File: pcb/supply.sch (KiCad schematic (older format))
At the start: 11 parts, among them J1 Barrel_Jack_Switch, J13 Conn_01x02_Female, U9 ZLDO1117G33TA

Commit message: added ice40 regulators
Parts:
- added C72, C76, C77: 33u, Capacitor_SMD:C_1206_3216Metric, symbol Device:C
- added C73: 10u, Capacitor_SMD:C_0805_2012Metric, symbol Device:C
- added C74, C75: 0.1u, Capacitor_SMD:C_0603_1608Metric, symbol Device:C
- added R2: 120, Resistor_SMD:R_0402_1005Metric, symbol Device:R
- added U18: ZLDO1117G33TA, SMD:SOT-223, symbol ZLDO1117G33TA:ZLDO1117G33TA
- added U19: ZLDO1117G12TA, symbol ZLDO1117G33TA:ZLDO1117G12TA
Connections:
- net labels added: 1V2_ICE, 3V3_ICE
- wire segments 21 -> 43
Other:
- note added: "1.2V ice40 regulator\n"
- note added: "3.3V ICE40 regulator\n"

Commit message: Added 3V3_STM in STM32F4 and supply sheets
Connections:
- net labels added: 3V3_STM
- net labels removed: 3V3_ESP
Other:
- note added: "STM regulator"
- note removed: "ESP32 regulator\n"
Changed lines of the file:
@@
 $EndComp
 Text Notes 9300 1050 0    50   ~ 0
-ESP32 regulator\n
+STM regulator
 $Comp
-L ventilator-PowerSymbols:3V3_ESP #PWR0165
+L ventilator-PowerSymbols:3V3_STM #PWR0165
 U 1 1 5E9883BE
 P 9850 1350
 F 0 "#PWR0165" H 9850 1310 30  0001 C CNN
-F 1 "3V3_ESP" H 9859 1488 30  0000 C CNN
+F 1 "3V3_STM" H 9859 1488 30  0000 C CNN
 F 2 "" H 9850 1350 60  0000 C CNN
 F 3 "" H 9850 1350 60  0000 C CNN

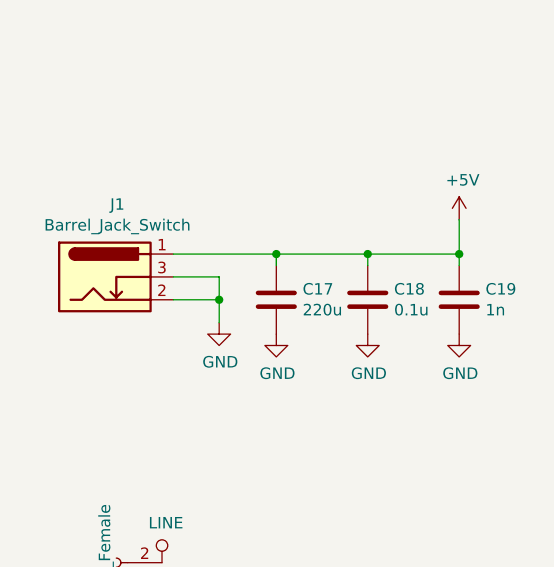
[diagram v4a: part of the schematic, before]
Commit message: stm32 jtag  connected
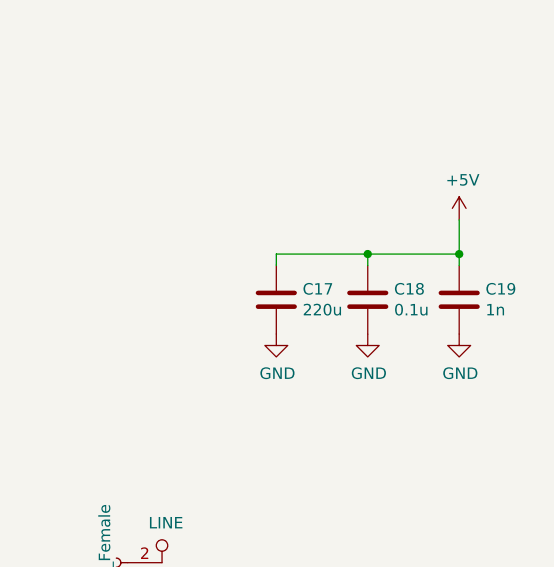
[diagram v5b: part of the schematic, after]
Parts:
- removed J1: Barrel_Jack_Switch, TH:BARREL_JACK, symbol BarrelConnector:Barrel_Jack_Switch
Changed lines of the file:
@@
 EESchema Schematic File Version 4
+LIBS:keep_breathing_ctrl-cache
 EELAYER 30 0
 EELAYER END
@@
 Comment4 ""
 $EndDescr
-$Comp
-L BarrelConnector:Barrel_Jack_Switch J?
-U 1 1 5E909FE7
-P 1700 1950
-AR Path="/5E909FE7" Ref="J?"  Part="1"
-AR Path="/5E8E60A3/5E909FE7" Ref="J1"  Part="1"
-F 0 "J1" H 1755 2267 50  0000 C CNN
-F 1 "Barrel_Jack_Switch" H 1755 2176 50  0000 C CNN
-F 2 "TH:BARREL_JACK" H 1750 1910 50  0001 C CNN
-F 3 "~" H 1750 1910 50  0001 C CNN
-F 4 "CP-002A-ND" H 1700 1950 50  0001 C CNN "DigiKey"
-	1    1700 1950
-	1    0    0    -1
-$EndComp
-Wire Wire Line
-	2000 1950 2200 1950
-Wire Wire Line
-	2200 1950 2200 2050
-Wire Wire Line
-	2200 2050 2000 2050
-$Comp
-L power:GND #PWR0106
-U 1 1 5E90A075
-P 2200 2150
-F 0 "#PWR0106" H 2200 1900 50  0001 C CNN
-F 1 "GND" H 2205 1977 50  0000 C CNN
-F 2 "" H 2200 2150 50  0001 C CNN
-F 3 "" H 2200 2150 50  0001 C CNN
-	1    2200 2150
-	1    0    0    -1
-$EndComp
-Wire Wire Line
-	2200 2150 2200 2050
-Connection ~ 2200 2050
 $Comp
 L Device:C C17
@@
 	3250 1900 3250 1850
 Wire Wire Line
-	2000 1850 2450 1850
-Wire Wire Line
 	2850 1900 2850 1850
 Connection ~ 2850 1850
@@
 Wire Wire Line
 	2450 1900 2450 1850
-Connection ~ 2450 1850
 Wire Wire Line
 	2450 1850 2850 1850

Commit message: small 1.2V reg
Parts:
- removed R2: 120, Resistor_SMD:R_0402_1005Metric, symbol Device:R
- removed U19: ZLDO1117G12TA, symbol ZLDO1117G33TA:ZLDO1117G12TA
- added U19: NCP177, SMD:XDFN4, symbol ncp177:NCP177
- C73: footprint Capacitor_SMD:C_0805_2012Metric -> Capacitor_SMD:C_0603_1608Metric
- C75: footprint Capacitor_SMD:C_0603_1608Metric -> Capacitor_SMD:C_0402_1005Metric
- C77: value 33u -> 1uF; footprint Capacitor_SMD:C_1206_3216Metric -> Capacitor_SMD:C_0603_1608Metric
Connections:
- net +5V: no longer C73.1
- net 1V2_ICE: now also U19.1 (OUT)
- net GND: now also U19.2 (GND), U19.EPAD
- new net +3V3: C73.1, U19.3 (EN), U19.4 (IN)
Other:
- moved on the sheet: C73, C75, C77
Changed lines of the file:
@@
 	6300 450  6300 6300
-$Comp
-L power:+5V #PWR0225
-U 1 1 5EA0A264
-P 7400 4950
-F 0 "#PWR0225" H 7400 4800 50  0001 C CNN
-F 1 "+5V" H 7415 5123 50  0000 C CNN
-F 2 "" H 7400 4950 50  0001 C CNN
-F 3 "" H 7400 4950 50  0001 C CNN
-	1    7400 4950
-	1    0    0    -1
-$EndComp
-$Comp
-L power:GND #PWR0226
-U 1 1 5EA0A26E
-P 8300 5600
-F 0 "#PWR0226" H 8300 5350 50  0001 C CNN
-F 1 "GND" H 8305 5427 50  0000 C CNN
-F 2 "" H 8300 5600 50  0001 C CNN
-F 3 "" H 8300 5600 50  0001 C CNN
-	1    8300 5600
-	1    0    0    -1
-$EndComp
-Wire Wire Line
-	9000 5250 9150 5250
-Wire Wire Line
-	9150 5250 9150 4950
-Wire Wire Line
-	9150 4950 9000 4950
-Wire Wire Line
-	10350 4950 10100 4950
-Connection ~ 9150 4950
 $Comp
 L Device:C C75
 U 1 1 5EA0A27E
-P 9300 5150
-F 0 "C75" H 9415 5196 50  0000 L CNN
-F 1 "0.1u" H 9415 5105 50  0000 L CNN
-F 2 "Capacitor_SMD:C_0603_1608Metric" H 9338 5000 50  0001 C CNN
-F 3 "~" H 9300 5150 50  0001 C CNN
-F 4 "720-1688-1-ND" H 9300 5150 50  0001 C CNN "DigiKey"
-	1    9300 5150
+P 8700 5175
+F 0 "C75" H 8815 5221 50  0000 L CNN
+F 1 "0.1u" H 8815 5130 50  0000 L CNN
+F 2 "Capacitor_SMD:C_0402_1005Metric" H 8738 5025 50  0001 C CNN
+F 3 "~" H 8700 5175 50  0001 C CNN
+F 4 "720-1688-1-ND" H 8700 5175 50  0001 C CNN "DigiKey"
+	1    8700 5175
 	1    0    0    -1
 $EndComp
@@
 L Device:C C77
 U 1 1 5EA0A289
-P 9700 5150
-F 0 "C77" H 9815 5196 50  0000 L CNN
-F 1 "33u" H 9815 5105 50  0000 L CNN
-F 2 "Capacitor_SMD:C_1206_3216Metric" H 9738 5000 50  0001 C CNN
-F 3 "~" H 9700 5150 50  0001 C CNN
-F 4 "445-14751-1-ND" H 9700 5150 50  0001 C CNN "DigiKey"
-	1    9700 5150
+P 9100 5175
+F 0 "C77" H 9215 5221 50  0000 L CNN
+F 1 "1uF" H 9215 5130 50  0000 L CNN
+F 2 "Capacitor_SMD:C_0603_1608Metric" H 9138 5025 50  0001 C CNN
+F 3 "~" H 9100 5175 50  0001 C CNN
+F 4 "445-14751-1-ND" H 9100 5175 50  0001 C CNN "DigiKey"
+	1    9100 5175
 	1    0    0    -1
 $EndComp
@@
 L Device:C C73
 U 1 1 5EA0A294
-P 7400 5250
-F 0 "C73" H 7515 5296 50  0000 L CNN
-F 1 "10u" H 7515 5205 50  0000 L CNN
-F 2 "Capacitor_SMD:C_0805_2012Metric" H 7438 5100 50  0001 C CNN
-F 3 "~" H 7400 5250 50  0001 C CNN
-F 4 "1276-6456-1-ND" H 7400 5250 50  0001 C CNN "DigiKey"
-	1    7400 5250
+P 7300 5075
+F 0 "C73" H 7415 5121 50  0000 L CNN
+F 1 "10u" H 7415 5030 50  0000 L CNN
+F 2 "Capacitor_SMD:C_0603_1608Metric" H 7338 4925 50  0001 C CNN
+F 3 "~" H 7300 5075 50  0001 C CNN
+F 4 "1276-6456-1-ND" H 7300 5075 50  0001 C CNN "DigiKey"
+	1    7300 5075
 	1    0    0    -1
 $EndComp
 Wire Wire Line
-	7600 5100 7400 5100
+	7300 4775 7300 4925
+Connection ~ 7300 4925
 Wire Wire Line
-	7400 4950 7400 5100
-Connection ~ 7400 5100
+	8700 5025 8700 4975
+Connection ~ 8700 4975
 Wire Wire Line
-	9300 5000 9300 4950
-Connection ~ 9300 4950
+	8700 4975 8550 4975
 Wire Wire Line
-	9300 4950 9150 4950
+	9100 5025 9100 4975
+Connection ~ 9100 4975
 Wire Wire Line
-	9700 5000 9700 4950
-Connection ~ 9700 4950
-Wire Wire Line
-	9700 4950 9300 4950
+	9100 4975 8700 4975
 $Comp
 L power:GND #PWR0227
 U 1 1 5EA0A2A7
-P 7400 5400
-F 0 "#PWR0227" H 7400 5150 50  0001 C CNN
-F 1 "GND" H 7405 5227 50  0000 C CNN
-F 2 "" H 7400 5400 50  0001 C CNN
-F 3 "" H 7400 5400 50  0001 C CNN
-	1    7400 5400
+P 7300 5225
+F 0 "#PWR0227" H 7300 4975 50  0001 C CNN
+F 1 "GND" H 7305 5052 50  0000 C CNN
+F 2 "" H 7300 5225 50  0001 C CNN
+F 3 "" H 7300 5225 50  0001 C CNN
+	1    7300 5225
 	1    0    0    -1
 $EndComp
@@
 L power:GND #PWR0228
 U 1 1 5EA0A2B1
-P 9300 5300
-F 0 "#PWR0228" H 9300 5050 50  0001 C CNN
-F 1 "GND" H 9305 5127 50  0000 C CNN
-F 2 "" H 9300 5300 50  0001 C CNN
-F 3 "" H 9300 5300 50  0001 C CNN
-	1    9300 5300
+P 8700 5325
+F 0 "#PWR0228" H 8700 5075 50  0001 C CNN
+F 1 "GND" H 8705 5152 50  0000 C CNN
+F 2 "" H 8700 5325 50  0001 C CNN
+F 3 "" H 8700 5325 50  0001 C CNN
+	1    8700 5325
 	1    0    0    -1
 $EndComp
@@
 L power:GND #PWR0229
 U 1 1 5EA0A2BB
-P 9700 5300
-F 0 "#PWR0229" H 9700 5050 50  0001 C CNN
-F 1 "GND" H 9705 5127 50  0000 C CNN
-F 2 "" H 9700 5300 50  0001 C CNN
-F 3 "" H 9700 5300 50  0001 C CNN
-	1    9700 5300
+P 9100 5325
+F 0 "#PWR0229" H 9100 5075 50  0001 C CNN
+F 1 "GND" H 9105 5152 50  0000 C CNN
+F 2 "" H 9100 5325 50  0001 C CNN
+F 3 "" H 9100 5325 50  0001 C CNN
+	1    9100 5325
 	1    0    0    -1
 $EndComp
@@
 L ventilator-PowerSymbols:1V2_ICE #PWR0230
 U 1 1 5EA0EA1D
-P 10350 4950
-F 0 "#PWR0230" H 10350 4910 30  0001 C CNN
-F 1 "1V2_ICE" H 10359 5088 30  0000 C CNN
-F 2 "" H 10350 4950 60  0000 C CNN
-F 3 "" H 10350 4950 60  0000 C CNN
-	1    10350 4950
+P 9750 4975
+F 0 "#PWR0230" H 9750 4935 30  0001 C CNN
+F 1 "1V2_ICE" H 9759 5113 30  0000 C CNN
+F 2 "" H 9750 4975 60  0000 C CNN
+F 3 "" H 9750 4975 60  0000 C CNN
+	1    9750 4975
 	1    0    0    -1
 $EndComp
 $Comp
-L ZLDO1117G33TA:ZLDO1117G12TA U19
-U 1 1 5EA0F149
-P 8300 5100
-F 0 "U19" H 8300 5587 60  0000 C CNN
-F 1 "ZLDO1117G12TA" H 8300 5481 60  0000 C CNN
-F 2 "" H 8450 5150 60  0000 C CNN
-F 3 "" H 8450 5150 60  0000 C CNN
-	1    8300 5100
+L ncp177:NCP177 U19
+U 1 1 5EA22602
+P 8150 5125
+F 0 "U19" H 8150 5550 50  0000 C CNN
+F 1 "NCP177" H 8150 5459 50  0000 C CNN
+F 2 "SMD:XDFN4" H 7900 5425 50  0001 C CNN
+F 3 "" H 7900 5425 50  0001 C CNN
+	1    8150 5125
+	1    0    0    -1
+$EndComp
+Wire Wire Line
+	9100 4975 9750 4975
+Wire Wire Line
+	7300 4925 7625 4925
+Wire Wire Line
+	7625 5125 7625 4925
+Connection ~ 7625 4925
+Wire Wire Line
+	7625 4925 7750 4925
+Wire Wire Line
+	7625 5125 7750 5125
+$Comp
+L power:+3V3 #PWR0225
+U 1 1 5EA2F978
+P 7300 4775
+F 0 "#PWR0225" H 7300 4625 50  0001 C CNN
+F 1 "+3V3" H 7315 4948 50  0000 C CNN
+F 2 "" H 7300 4775 50  0001 C CNN
+F 3 "" H 7300 4775 50  0001 C CNN
+	1    7300 4775
 	1    0    0    -1
 $EndComp
 $Comp
-L Device:R R2
-U 1 1 5EA113A0
-P 10100 5150
-F 0 "R2" H 10170 5196 50  0000 L CNN
-F 1 "120" H 10170 5105 50  0000 L CNN
-F 2 "Resistor_SMD:R_0402_1005Metric" V 10030 5150 50  0001 C CNN
-F 3 "~" H 10100 5150 50  0001 C CNN
-	1    10100 5150
+L power:GND #PWR0226
+U 1 1 5EA31ABA
+P 8200 5525
+F 0 "#PWR0226" H 8200 5275 50  0001 C CNN
+F 1 "GND" H 8205 5352 50  0000 C CNN
+F 2 "" H 8200 5525 50  0001 C CNN
+F 3 "" H 8200 5525 50  0001 C CNN
+	1    8200 5525
 	1    0    0    -1
 $EndComp
 Wire Wire Line
-	10100 5000 10100 4950
-Connection ~ 10100 4950
+	8100 5475 8200 5475
 Wire Wire Line
-	10100 4950 9700 4950
-$Comp
-L power:GND #PWR0231
-U 1 1 5EA127C0
-P 10100 5300
-F 0 "#PWR0231" H 10100 5050 50  0001 C CNN
-F 1 "GND" H 10105 5127 50  0000 C CNN
-F 2 "" H 10100 5300 50  0001 C CNN
-F 3 "" H 10100 5300 50  0001 C CNN
-	1    10100 5300
-	1    0    0    -1
-$EndComp
+	8200 5475 8200 5525
+Connection ~ 8200 5475
 $EndSCHEMATC

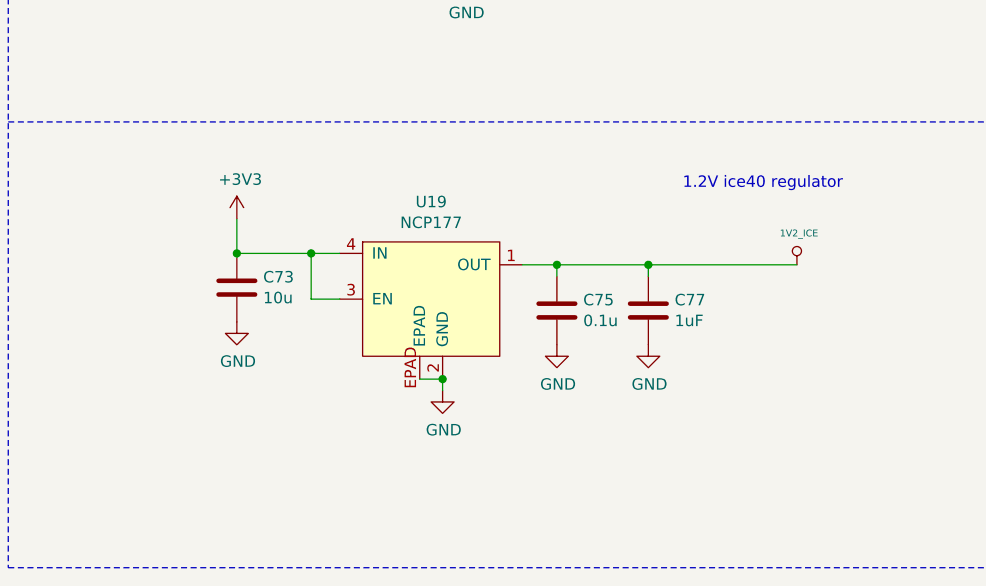
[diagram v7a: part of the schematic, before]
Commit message: 1.2v ldo changed
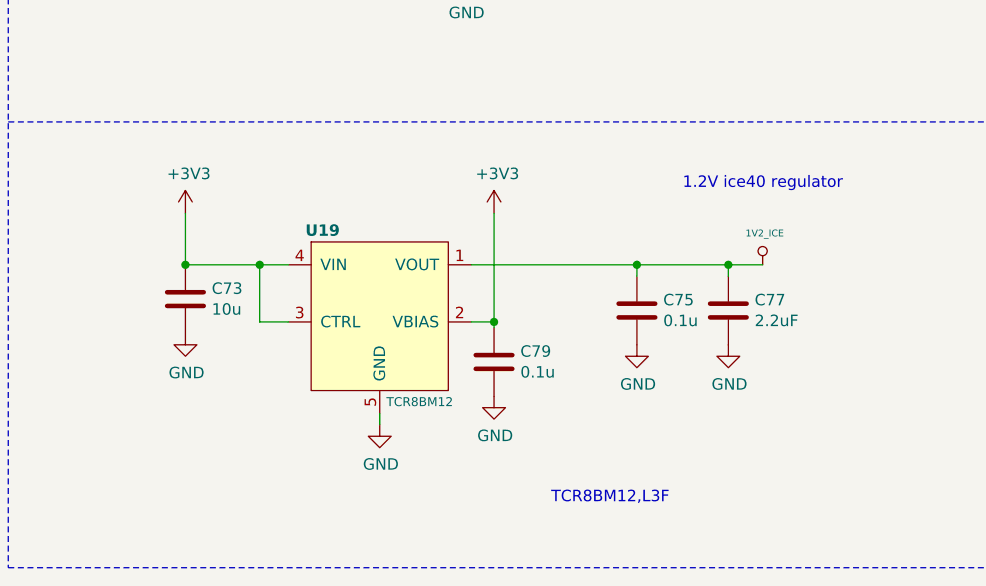
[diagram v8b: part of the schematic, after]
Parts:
- removed U19: NCP177, SMD:XDFN4, symbol ncp177:NCP177
- added C79: 0.1u, Capacitor_SMD:C_0402_1005Metric, symbol Device:C
- added U19: TCR8BM12, symbol TCR8BM12:TCR8BM12
- C77: value 1uF -> 2.2uF
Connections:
- net +3V3: now also C79.1, U19.2 (VBIAS), U19.3 (CTRL), U19.4 (VIN)
- net 1V2_ICE: now also U19.1 (VOUT)
- net GND: now also C79.2, U19.5 (GND)
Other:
- note added: "TCR8BM12,L3F"
- moved on the sheet: C73, C75, C77
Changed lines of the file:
@@
 L Device:C C75
 U 1 1 5EA0A27E
-P 8700 5175
-F 0 "C75" H 8815 5221 50  0000 L CNN
-F 1 "0.1u" H 8815 5130 50  0000 L CNN
-F 2 "Capacitor_SMD:C_0402_1005Metric" H 8738 5025 50  0001 C CNN
-F 3 "~" H 8700 5175 50  0001 C CNN
-F 4 "720-1688-1-ND" H 8700 5175 50  0001 C CNN "DigiKey"
-	1    8700 5175
+P 9050 5175
+F 0 "C75" H 9165 5221 50  0000 L CNN
+F 1 "0.1u" H 9165 5130 50  0000 L CNN
+F 2 "Capacitor_SMD:C_0402_1005Metric" H 9088 5025 50  0001 C CNN
+F 3 "~" H 9050 5175 50  0001 C CNN
+F 4 "720-1688-1-ND" H 9050 5175 50  0001 C CNN "DigiKey"
+	1    9050 5175
 	1    0    0    -1
 $EndComp
@@
 L Device:C C77
 U 1 1 5EA0A289
-P 9100 5175
-F 0 "C77" H 9215 5221 50  0000 L CNN
-F 1 "1uF" H 9215 5130 50  0000 L CNN
-F 2 "Capacitor_SMD:C_0603_1608Metric" H 9138 5025 50  0001 C CNN
-F 3 "~" H 9100 5175 50  0001 C CNN
-F 4 "445-14751-1-ND" H 9100 5175 50  0001 C CNN "DigiKey"
-	1    9100 5175
+P 9450 5175
+F 0 "C77" H 9565 5221 50  0000 L CNN
+F 1 "2.2uF" H 9565 5130 50  0000 L CNN
+F 2 "Capacitor_SMD:C_0603_1608Metric" H 9488 5025 50  0001 C CNN
+F 3 "~" H 9450 5175 50  0001 C CNN
+F 4 "445-14751-1-ND" H 9450 5175 50  0001 C CNN "DigiKey"
+	1    9450 5175
 	1    0    0    -1
 $EndComp
@@
 L Device:C C73
 U 1 1 5EA0A294
-P 7300 5075
-F 0 "C73" H 7415 5121 50  0000 L CNN
-F 1 "10u" H 7415 5030 50  0000 L CNN
-F 2 "Capacitor_SMD:C_0603_1608Metric" H 7338 4925 50  0001 C CNN
-F 3 "~" H 7300 5075 50  0001 C CNN
-F 4 "1276-6456-1-ND" H 7300 5075 50  0001 C CNN "DigiKey"
-	1    7300 5075
+P 7075 5125
+F 0 "C73" H 7190 5171 50  0000 L CNN
+F 1 "10u" H 7190 5080 50  0000 L CNN
+F 2 "Capacitor_SMD:C_0603_1608Metric" H 7113 4975 50  0001 C CNN
+F 3 "~" H 7075 5125 50  0001 C CNN
+F 4 "1276-6456-1-ND" H 7075 5125 50  0001 C CNN "DigiKey"
+	1    7075 5125
 	1    0    0    -1
 $EndComp
 Wire Wire Line
-	7300 4775 7300 4925
-Connection ~ 7300 4925
+	7075 4750 7075 4975
+Connection ~ 7075 4975
 Wire Wire Line
-	8700 5025 8700 4975
-Connection ~ 8700 4975
+	9050 5025 9050 4975
+Connection ~ 9050 4975
 Wire Wire Line
-	8700 4975 8550 4975
+	9450 5025 9450 4975
+Connection ~ 9450 4975
 Wire Wire Line
-	9100 5025 9100 4975
-Connection ~ 9100 4975
-Wire Wire Line
-	9100 4975 8700 4975
+	9450 4975 9050 4975
 $Comp
 L power:GND #PWR0227
 U 1 1 5EA0A2A7
-P 7300 5225
-F 0 "#PWR0227" H 7300 4975 50  0001 C CNN
-F 1 "GND" H 7305 5052 50  0000 C CNN
-F 2 "" H 7300 5225 50  0001 C CNN
-F 3 "" H 7300 5225 50  0001 C CNN
-	1    7300 5225
+P 7075 5275
+F 0 "#PWR0227" H 7075 5025 50  0001 C CNN
+F 1 "GND" H 7080 5102 50  0000 C CNN
+F 2 "" H 7075 5275 50  0001 C CNN
+F 3 "" H 7075 5275 50  0001 C CNN
+	1    7075 5275
 	1    0    0    -1
 $EndComp
@@
 L power:GND #PWR0228
 U 1 1 5EA0A2B1
-P 8700 5325
-F 0 "#PWR0228" H 8700 5075 50  0001 C CNN
-F 1 "GND" H 8705 5152 50  0000 C CNN
-F 2 "" H 8700 5325 50  0001 C CNN
-F 3 "" H 8700 5325 50  0001 C CNN
-	1    8700 5325
+P 9050 5325
+F 0 "#PWR0228" H 9050 5075 50  0001 C CNN
+F 1 "GND" H 9055 5152 50  0000 C CNN
+F 2 "" H 9050 5325 50  0001 C CNN
+F 3 "" H 9050 5325 50  0001 C CNN
+	1    9050 5325
 	1    0    0    -1
 $EndComp
@@
 L power:GND #PWR0229
 U 1 1 5EA0A2BB
-P 9100 5325
-F 0 "#PWR0229" H 9100 5075 50  0001 C CNN
-F 1 "GND" H 9105 5152 50  0000 C CNN
-F 2 "" H 9100 5325 50  0001 C CNN
-F 3 "" H 9100 5325 50  0001 C CNN
-	1    9100 5325
+P 9450 5325
+F 0 "#PWR0229" H 9450 5075 50  0001 C CNN
+F 1 "GND" H 9455 5152 50  0000 C CNN
+F 2 "" H 9450 5325 50  0001 C CNN
+F 3 "" H 9450 5325 50  0001 C CNN
+	1    9450 5325
 	1    0    0    -1
 $EndComp
@@
 L ventilator-PowerSymbols:1V2_ICE #PWR0230
 U 1 1 5EA0EA1D
-P 9750 4975
-F 0 "#PWR0230" H 9750 4935 30  0001 C CNN
-F 1 "1V2_ICE" H 9759 5113 30  0000 C CNN
-F 2 "" H 9750 4975 60  0000 C CNN
-F 3 "" H 9750 4975 60  0000 C CNN
-	1    9750 4975
-	1    0    0    -1
-$EndComp
-$Comp
-L ncp177:NCP177 U19
-U 1 1 5EA22602
-P 8150 5125
-F 0 "U19" H 8150 5550 50  0000 C CNN
-F 1 "NCP177" H 8150 5459 50  0000 C CNN
-F 2 "SMD:XDFN4" H 7900 5425 50  0001 C CNN
-F 3 "" H 7900 5425 50  0001 C CNN
-	1    8150 5125
+P 9600 4975
+F 0 "#PWR0230" H 9600 4935 30  0001 C CNN
+F 1 "1V2_ICE" H 9609 5113 30  0000 C CNN
+F 2 "" H 9600 4975 60  0000 C CNN
+F 3 "" H 9600 4975 60  0000 C CNN
+	1    9600 4975
 	1    0    0    -1
 $EndComp
 Wire Wire Line
-	9100 4975 9750 4975
+	9450 4975 9600 4975
 Wire Wire Line
-	7300 4925 7625 4925
+	7075 4975 7400 4975
+Connection ~ 7400 4975
 Wire Wire Line
-	7625 5125 7625 4925
-Connection ~ 7625 4925
-Wire Wire Line
-	7625 4925 7750 4925
-Wire Wire Line
-	7625 5125 7750 5125
+	7400 4975 7525 4975
 $Comp
 L power:+3V3 #PWR0225
 U 1 1 5EA2F978
-P 7300 4775
-F 0 "#PWR0225" H 7300 4625 50  0001 C CNN
-F 1 "+3V3" H 7315 4948 50  0000 C CNN
-F 2 "" H 7300 4775 50  0001 C CNN
-F 3 "" H 7300 4775 50  0001 C CNN
-	1    7300 4775
+P 7075 4750
+F 0 "#PWR0225" H 7075 4600 50  0001 C CNN
+F 1 "+3V3" H 7090 4923 50  0000 C CNN
+F 2 "" H 7075 4750 50  0001 C CNN
+F 3 "" H 7075 4750 50  0001 C CNN
+	1    7075 4750
 	1    0    0    -1
 $EndComp
@@
 L power:GND #PWR0226
 U 1 1 5EA31ABA
-P 8200 5525
-F 0 "#PWR0226" H 8200 5275 50  0001 C CNN
-F 1 "GND" H 8205 5352 50  0000 C CNN
-F 2 "" H 8200 5525 50  0001 C CNN
-F 3 "" H 8200 5525 50  0001 C CNN
-	1    8200 5525
+P 7925 5675
+F 0 "#PWR0226" H 7925 5425 50  0001 C CNN
+F 1 "GND" H 7930 5502 50  0000 C CNN
+F 2 "" H 7925 5675 50  0001 C CNN
+F 3 "" H 7925 5675 50  0001 C CNN
+	1    7925 5675
 	1    0    0    -1
 $EndComp
 Wire Wire Line
-	8100 5475 8200 5475
+	7925 5625 7925 5675
+Text Notes 8675 6025 0    50   ~ 0
+ TCR8BM12,L3F
+$Comp
+L TCR8BM12:TCR8BM12 U19
+U 1 1 5EA68891
+P 7975 5125
+F 0 "U19" H 7675 5425 50  0000 C CNB
+F 1 "TCR8BM12" H 8100 4675 39  0000 C CNN
+F 2 "" H 7925 5125 50  0001 C CNN
+F 3 "" H 7925 5125 50  0001 C CNN
+F 4 " TCR8BM12L3FDKR-ND " H 7975 5125 50  0001 C CNN "DigiKey"
+	1    7975 5125
+	1    0    0    -1
+$EndComp
 Wire Wire Line
-	8200 5475 8200 5525
-Connection ~ 8200 5475
+	7525 5225 7400 5225
+Wire Wire Line
+	7400 4975 7400 5225
+$Comp
+L Device:C C79
+U 1 1 5EA84E78
+P 8425 5400
+F 0 "C79" H 8540 5446 50  0000 L CNN
+F 1 "0.1u" H 8540 5355 50  0000 L CNN
+F 2 "Capacitor_SMD:C_0402_1005Metric" H 8463 5250 50  0001 C CNN
+F 3 "~" H 8425 5400 50  0001 C CNN
+F 4 "720-1688-1-ND" H 8425 5400 50  0001 C CNN "DigiKey"
+	1    8425 5400
+	1    0    0    -1
+$EndComp
+$Comp
+L power:GND #PWR0231
+U 1 1 5EA84E82
+P 8425 5550
+F 0 "#PWR0231" H 8425 5300 50  0001 C CNN
+F 1 "GND" H 8430 5377 50  0000 C CNN
+F 2 "" H 8425 5550 50  0001 C CNN
+F 3 "" H 8425 5550 50  0001 C CNN
+	1    8425 5550
+	1    0    0    -1
+$EndComp
+Wire Wire Line
+	8325 4975 9050 4975
+Wire Wire Line
+	8325 5225 8425 5225
+Wire Wire Line
+	8425 5225 8425 5250
+$Comp
+L power:+3V3 #PWR?
+U 1 1 5EA99800
+P 8425 4750
+F 0 "#PWR?" H 8425 4600 50  0001 C CNN
+F 1 "+3V3" H 8440 4923 50  0000 C CNN
+F 2 "" H 8425 4750 50  0001 C CNN
+F 3 "" H 8425 4750 50  0001 C CNN
+	1    8425 4750
+	1    0    0    -1
+$EndComp
+Wire Wire Line
+	8425 4750 8425 5225
+Connection ~ 8425 5225
 $EndSCHEMATC
